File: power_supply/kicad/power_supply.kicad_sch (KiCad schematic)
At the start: 16 parts, among them J1 pcie_98, J2 Conn_01x05_Socket, U1 URB2405YMD-10WR3, U2 ESD5344D

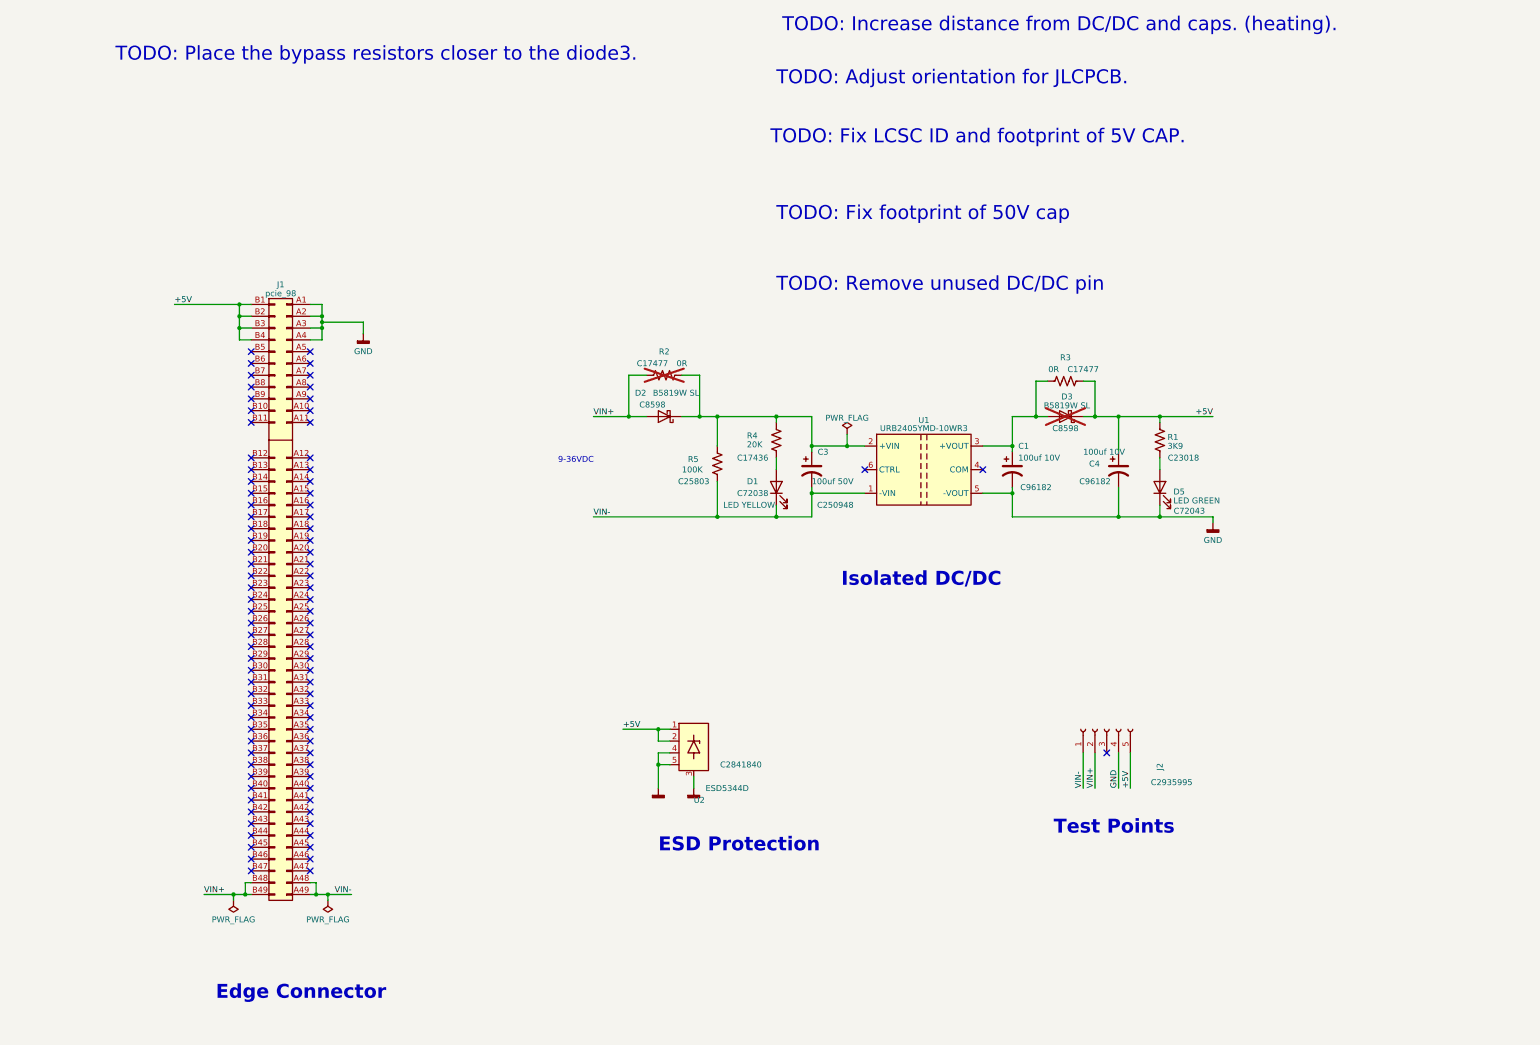
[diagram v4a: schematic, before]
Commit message: Tweaked the power supply PCB: arranged silkscreen labels, rotated the ESD device.
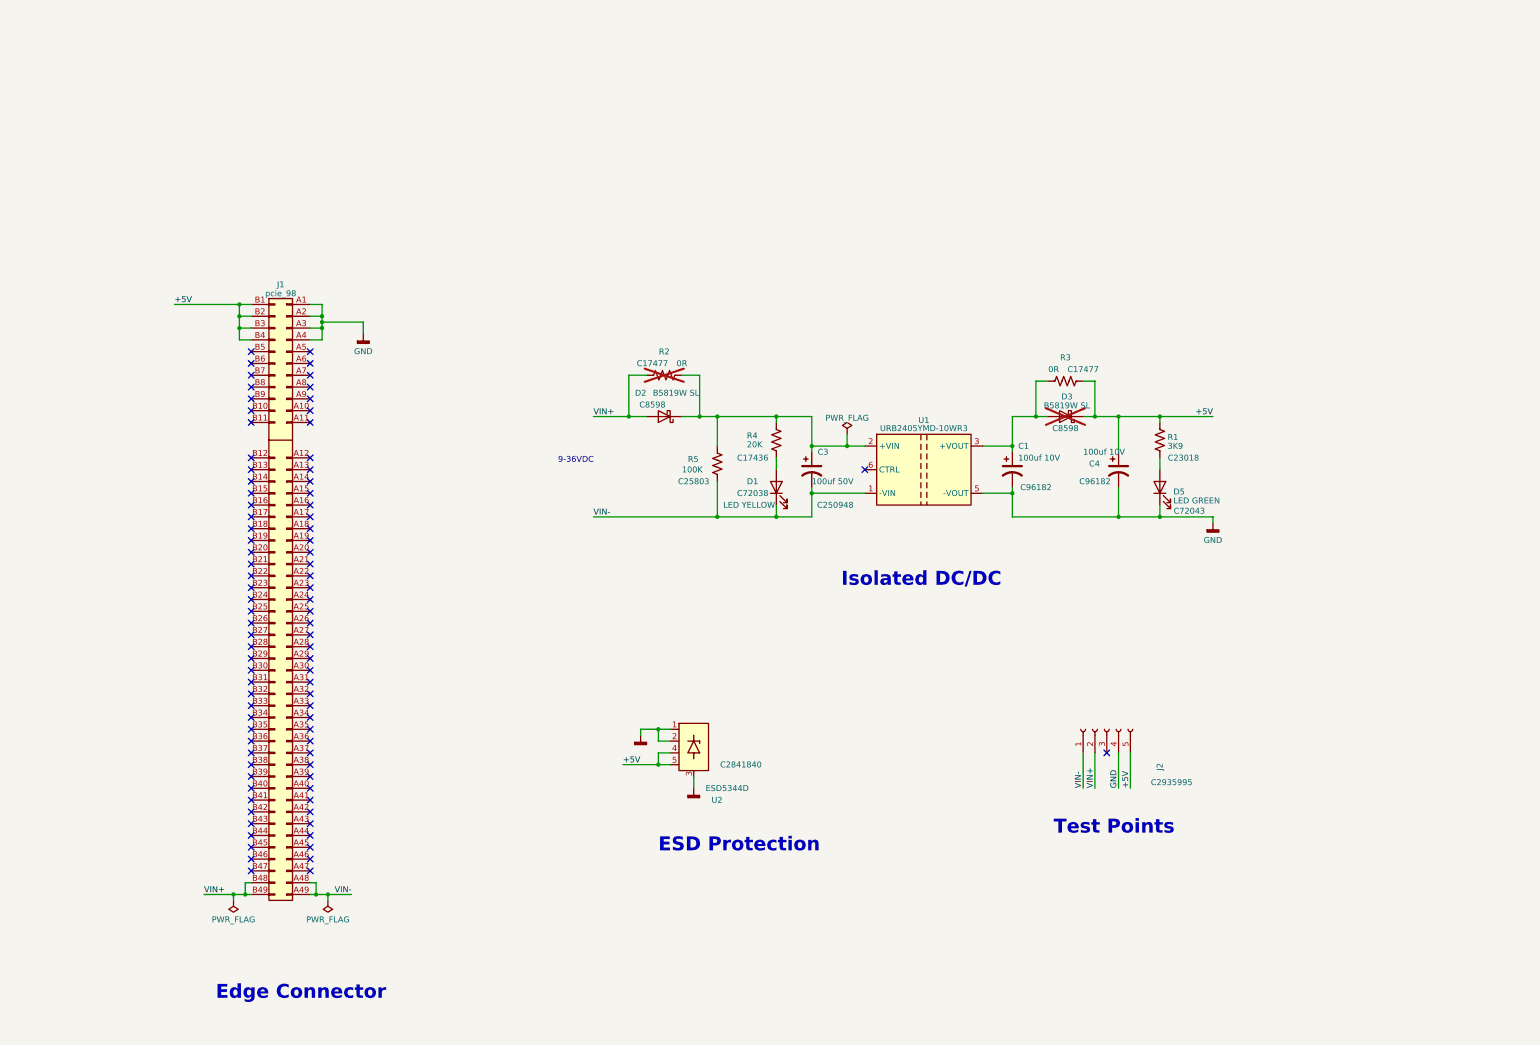
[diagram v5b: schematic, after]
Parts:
- C1, C4: footprint power_supply:CP_Elec_5x5.4_JLCPCB -> Capacitor_SMD:CP_Elec_5x5.4
- C3: footprint power_supply:C_Elec_8x10.2_JLCPCB -> Capacitor_SMD:C_Elec_8x10.2
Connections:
- net +5V: now also U2.4 (D3), U2.5 (D4); no longer U2.1 (D1), U2.2 (D2)
- net GND: now also U2.1 (D1), U2.2 (D2); no longer U2.4 (D3), U2.5 (D4)
- no-connect marks 89 -> 88
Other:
- note removed: "TODO: Adjust orientation for JLCPCB."
- note removed: "TODO: Fix LCSC ID and footprint of 5V CAP."
- note removed: "TODO: Fix footprint of 50V cap"
- note removed: "TODO: Increase distance from DC/DC and caps. (heating)."
- note removed: "TODO: Place the bypass resistors closer to the diode3."
- note removed: "TODO: Remove unused DC/DC pin"
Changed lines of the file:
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@@
   (junction (at 101.6 203.2) (diameter 0) (color 0 0 0 0)
   )
+  (junction (at 172.72 175.26) (diameter 0) (color 0 0 0 0)
+  )
   (junction (at 248.92 106.68) (diameter 0) (color 0 0 0 0)
   )
@@
   )
   (junction (at 205.74 116.84) (diameter 0) (color 0 0 0 0)
-  )
-  (junction (at 172.72 175.26) (diameter 0) (color 0 0 0 0)
   )
   (junction (at 172.72 167.64) (diameter 0) (color 0 0 0 0)
@@
   (no_connect (at 85.09 137.16))
   (no_connect (at 97.79 99.06))
-  (no_connect (at 242.57 111.76))
   (no_connect (at 97.79 152.4))
   (no_connect (at 97.79 142.24))
@@
     (stroke (width 0) (type default))
   )
+  (wire (pts (xy 165.1 175.26) (xy 172.72 175.26))
+    (stroke (width 0) (type default))
+  )
   (wire (pts (xy 248.92 121.92) (xy 248.92 116.84))
     (stroke (width 0) (type default))
@@
     (stroke (width 0) (type default))
   )
-  (wire (pts (xy 165.1 167.64) (xy 172.72 167.64))
+  (wire (pts (xy 168.91 167.64) (xy 172.72 167.64))
     (stroke (width 0) (type default))
   )
@@
     (stroke (width 0) (type default))
   )
-  (wire (pts (xy 172.72 175.26) (xy 172.72 180.34))
-    (stroke (width 0) (type default))
-  )
   (wire (pts (xy 172.72 175.26) (xy 175.26 175.26))
     (stroke (width 0) (type default))
@@
   )
   (wire (pts (xy 68.58 76.2) (xy 82.55 76.2))
+    (stroke (width 0) (type default))
+  )
+  (wire (pts (xy 168.91 167.64) (xy 168.91 168.91))
     (stroke (width 0) (type default))
   )
@@
     (effects (font (size 3 3) (thickness 0.6) bold) (justify left bottom))
   )
-  (text "TODO: Fix LCSC ID and footprint of 5V CAP." (at 196.85 41.91 0)
-    (effects (font (size 3 3) (color 255 0 0 1)) (justify left bottom))
-  )
-  (text "TODO: Increase distance from DC/DC and caps. (heating)."
-    (at 199.39 17.78 0)
-    (effects (font (size 3 3) (color 255 0 0 1)) (justify left bottom))
-  )
   (text "9-36VDC" (at 151.13 110.49 0)
     (effects (font (size 1.27 1.27)) (justify left bottom))
@@
     (effects (font (size 3 3) (thickness 0.6) bold) (justify left bottom))
   )
-  (text "TODO: Remove unused DC/DC pin" (at 198.12 73.66 0)
-    (effects (font (size 3 3) (color 255 0 0 1)) (justify left bottom))
-  )
   (text "Isolated DC/DC" (at 212.09 137.16 0)
     (effects (font (size 3 3) (thickness 0.6) bold) (justify left bottom))
   )
-  (text "TODO: Adjust orientation for JLCPCB." (at 198.12 29.21 0)
-    (effects (font (size 3 3) (color 255 0 0 1)) (justify left bottom))
-  )
   (text "Test Points" (at 257.81 190.5 0)
     (effects (font (size 3 3) (thickness 0.6) bold) (justify left bottom))
   )
-  (text "TODO: Place the bypass resistors closer to the diode3."
-    (at 55.88 24.13 0)
-    (effects (font (size 3 3) (color 255 0 0 1)) (justify left bottom))
-  )
-  (text "TODO: Fix footprint of 50V cap" (at 198.12 58.42 0)
-    (effects (font (size 3 3) (color 255 0 0 1)) (justify left bottom))
-  )
   (label "VIN+" (at 158.75 100.33 0) (fields_autoplaced)
     (effects (font (size 1.27 1.27)) (justify left bottom))
   )
-  (label "+5V" (at 165.1 167.64 0) (fields_autoplaced)
+  (label "+5V" (at 165.1 175.26 0) (fields_autoplaced)
     (effects (font (size 1.27 1.27)) (justify left bottom))
   )
@@
       (effects (font (size 1.27 1.27)) (justify left))
     )
-    (property "Footprint" "power_supply:CP_Elec_5x5.4_JLCPCB" (at 271.78 111.76 0)
+    (property "Footprint" "Capacitor_SMD:CP_Elec_5x5.4" (at 271.78 111.76 0)
       (effects (font (size 1.27 1.27)) hide)
     )
@@
       (effects (font (size 1.27 1.27)) (justify left))
     )
-    (property "Footprint" "power_supply:CP_Elec_5x5.4_JLCPCB" (at 248.92 111.76 0)
+    (property "Footprint" "Capacitor_SMD:CP_Elec_5x5.4" (at 248.92 111.76 0)
       (effects (font (size 1.27 1.27)) hide)
     )
@@
     (pin "2")
     (pin "3")
-    (pin "4")
     (pin "5")
     (pin "6")
@@
   (symbol (lib_id "power_supply:ESD5344D") (at 180.34 172.72 0) (unit 1)
     (in_bom yes) (on_board yes) (dnp no)
-    (property "Reference" "U2" (at 180.34 182.88 0)
+    (property "Reference" "U2" (at 184.15 182.88 0)
       (effects (font (size 1.27 1.27)) (justify left))
     )
@@
     )
   )
-  (symbol (lib_id "power_supply:GND") (at 172.72 180.34 0) (unit 1)
+  (symbol (lib_id "Device:R_US") (at 280.67 105.41 0) (unit 1)
+    (in_bom yes) (on_board yes) (dnp no)
+    (property "Reference" "R1" (at 282.321 104.7663 0)
+      (effects (font (size 1.27 1.27)) (justify left))
+    )
+    (property "Value" "3K9" (at 282.321 106.6873 0)
+      (effects (font (size 1.27 1.27)) (justify left))
+    )
+    (property "Footprint" "Resistor_SMD:R_0603_1608Metric" (at 281.686 105.664 90)
+      (effects (font (size 1.27 1.27)) hide)
+    )
+    (property "Datasheet" "~" (at 280.67 105.41 0)
+      (effects (font (size 1.27 1.27)) hide)
+    )
+    (property "LCSC" "C23018" (at 285.75 109.22 0)
+      (effects (font (size 1.27 1.27)))
+    )
+    (pin "1")
+    (pin "2")
+    (instances
+      (project "power_supply"
+        (path "/0dcd9c8c-bd5a-437f-856e-101fb6cf8b66"
+          (reference "R1") (unit 1)
+        )
+      )
+    )
+  )
+  (symbol (lib_id "power_supply:GND") (at 168.91 168.91 0) (unit 1)
     (in_bom yes) (on_board yes) (dnp no) (fields_autoplaced)
-    (property "Reference" "#PWR03" (at 172.72 186.69 0)
-      (effects (font (size 1.27 1.27)) hide)
-    )
-    (property "Value" "GND" (at 172.72 184.0945 0)
-      (effects (font (size 1.27 1.27)) hide)
-    )
-    (property "Footprint" "" (at 172.72 180.34 0)
-      (effects (font (size 1.27 1.27)) hide)
-    )
-    (property "Datasheet" "" (at 172.72 180.34 0)
+    (property "Reference" "#PWR03" (at 168.91 175.26 0)
+      (effects (font (size 1.27 1.27)) hide)
+    )
+    (property "Value" "GND" (at 168.91 172.6645 0)
+      (effects (font (size 1.27 1.27)) hide)
+    )
+    (property "Footprint" "" (at 168.91 168.91 0)
+      (effects (font (size 1.27 1.27)) hide)
+    )
+    (property "Datasheet" "" (at 168.91 168.91 0)
       (effects (font (size 1.27 1.27)) hide)
     )
@@
         (path "/0dcd9c8c-bd5a-437f-856e-101fb6cf8b66"
           (reference "#PWR03") (unit 1)
-        )
-      )
-    )
-  )
-  (symbol (lib_id "Device:R_US") (at 280.67 105.41 0) (unit 1)
-    (in_bom yes) (on_board yes) (dnp no)
-    (property "Reference" "R1" (at 282.321 104.7663 0)
-      (effects (font (size 1.27 1.27)) (justify left))
-    )
-    (property "Value" "3K9" (at 282.321 106.6873 0)
-      (effects (font (size 1.27 1.27)) (justify left))
-    )
-    (property "Footprint" "Resistor_SMD:R_0603_1608Metric" (at 281.686 105.664 90)
-      (effects (font (size 1.27 1.27)) hide)
-    )
-    (property "Datasheet" "~" (at 280.67 105.41 0)
-      (effects (font (size 1.27 1.27)) hide)
-    )
-    (property "LCSC" "C23018" (at 285.75 109.22 0)
-      (effects (font (size 1.27 1.27)))
-    )
-    (pin "1")
-    (pin "2")
-    (instances
-      (project "power_supply"
-        (path "/0dcd9c8c-bd5a-437f-856e-101fb6cf8b66"
-          (reference "R1") (unit 1)
         )
       )
@@
       (effects (font (size 1.27 1.27)) (justify left))
     )
-    (property "Footprint" "power_supply:C_Elec_8x10.2_JLCPCB" (at 205.74 111.76 0)
-      (effects (font (size 1.27 1.27)) hide)
-    )
+    (property "Footprint" "Capacitor_SMD:C_Elec_8x10.2" (at 205.74 111.76 0)
+      (effects (font (size 1.27 1.27)) hide)
+    )

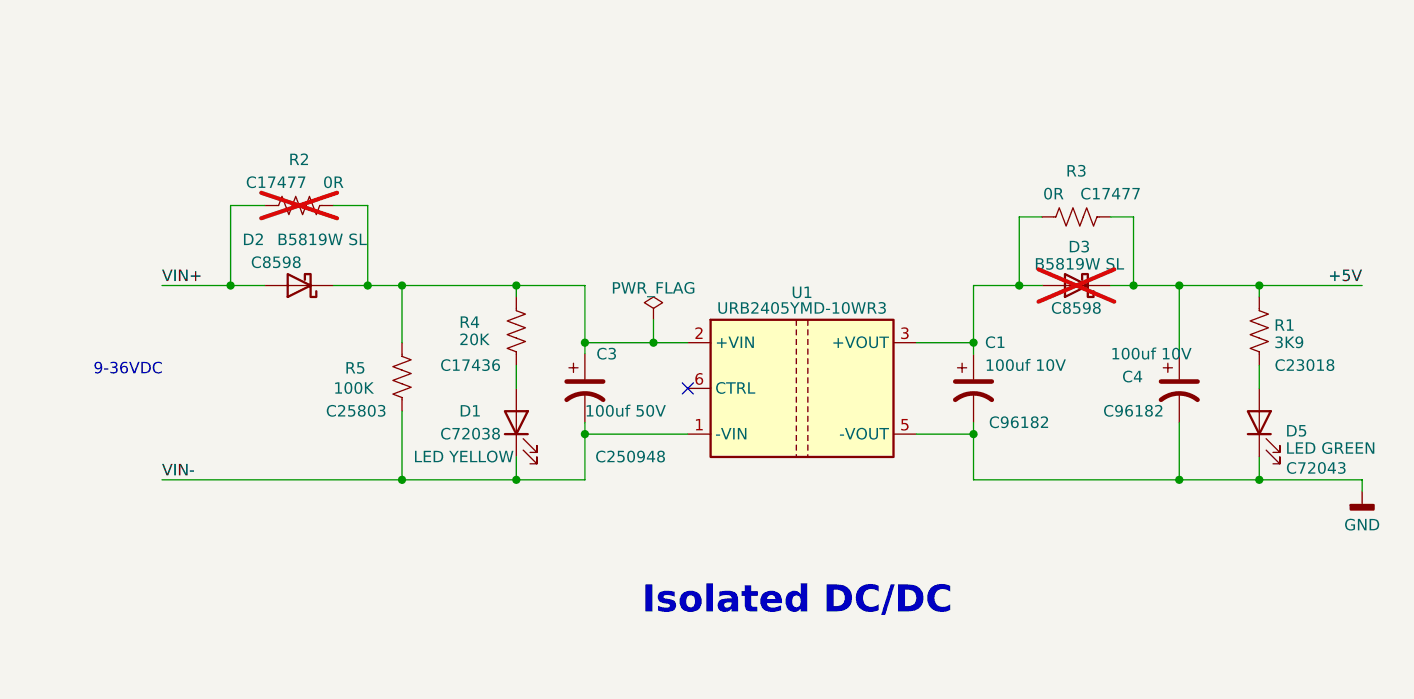
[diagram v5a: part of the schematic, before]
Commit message: Simplified the power supply. Removed jumper resistors and output diode. Replaced reverse current leakage resistor with a diode.
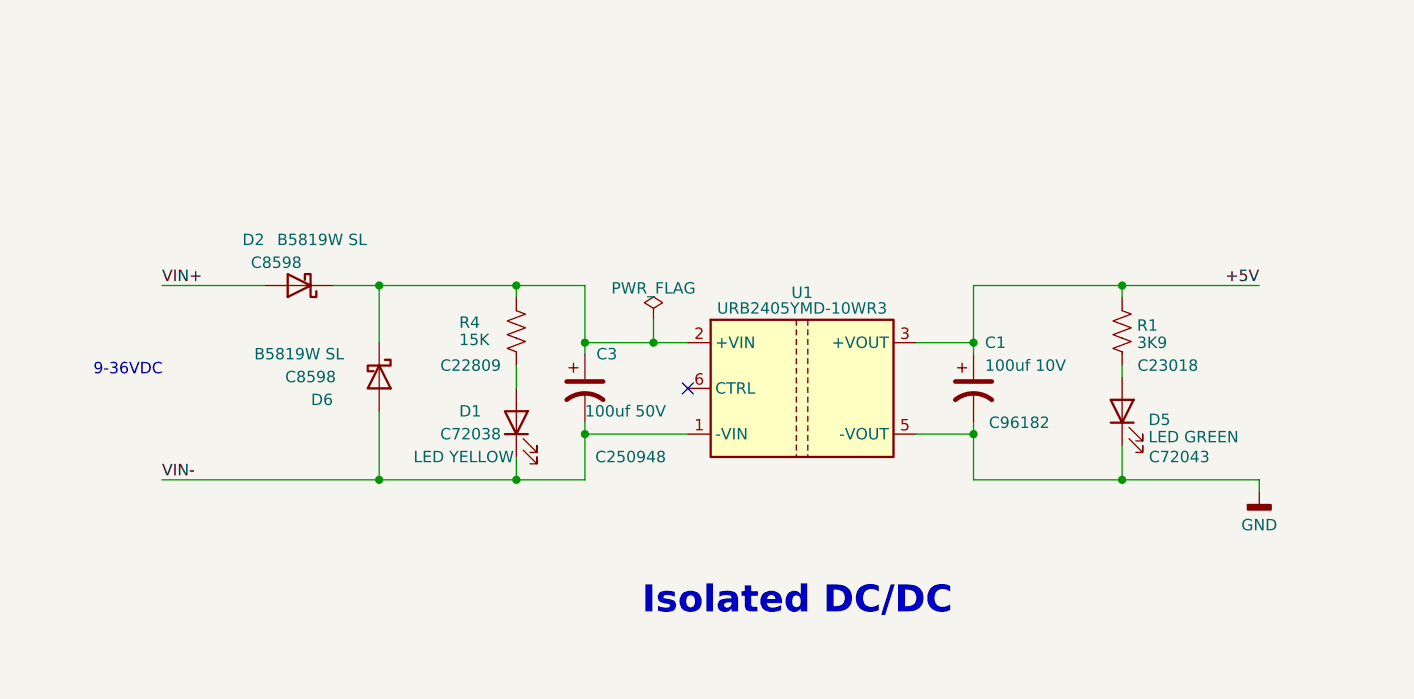
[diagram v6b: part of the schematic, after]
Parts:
- removed C4: 100uf 10V, Capacitor_SMD:CP_Elec_5x5.4, symbol Device:C_Polarized_US
- removed D3: B5819W SL, Diode_SMD:D_SOD-123, symbol Device:D_Schottky
- removed R2, R3: 0R, Resistor_SMD:R_0805_2012Metric, symbol Device:R_US
- removed R5: 100K, Resistor_SMD:R_0603_1608Metric, symbol Device:R_US
- added D6: B5819W SL, Diode_SMD:D_SOD-123, symbol Device:D_Schottky
- R4: value 20K -> 15K; LCSC C17436 -> C22809
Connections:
- net +5V: now also C1.1, U1.3 (+VOUT)
- net VIN-: now also D6.2 (A)
- net at C3.1, D2.1 (K), R4.1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: now also D6.1 (K)
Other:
- moved on the sheet: D5, R1

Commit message: More power supply pcb cleanup
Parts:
- added F1, F2: 1.25A, Fuse:Fuse_1206_3216Metric, symbol Device:Fuse_Small
- added F3: 2A, Fuse:Fuse_1206_3216Metric, symbol Device:Fuse_Small
- added R2, R3, R5, R6: 1K, Resistor_SMD:R_0603_1608Metric, symbol Device:R_US
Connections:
- net +5V: now also F3.2, R6.2; no longer C1.1, J2.5 (Pin_5), U1.3 (+VOUT)
- net GND: now also R5.2; no longer J2.4 (Pin_4)
- net VIN+: now also F1.1, R3.2; no longer D2.2 (A), J2.2 (Pin_2)
- net VIN-: now also F2.1, R2.2; no longer C3.2, D1.1 (K), D6.2 (A), J2.1 (Pin_1), U1.1 (-VIN)
- new net: C3.2, D1.1 (K), D6.2 (A), F2.2, U1.1 (-VIN)
- new net: C1.1, F3.1, U1.3 (+VOUT)
- new net: D2.2 (A), F1.2
- new net: J2.2 (Pin_2), R3.1
- new net: J2.1 (Pin_1), R2.1
- new net: J2.4 (Pin_4), R5.1
- new net: J2.5 (Pin_5), R6.1
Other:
- note added: "9-36VDC 12W"
- note removed: "9-36VDC"
- moved on the sheet: D5, R1, U2
